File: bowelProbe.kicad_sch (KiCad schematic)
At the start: 89 parts, among them J1 Conn_01x01, J10 Conn_01x01, J11 Conn_02x03_Odd_Even, J12 Conn_01x01, J13 Conn_01x01, J2 Conn_01x01, J3 Conn_01x08, J4 Conn_01x08, J5 Conn_01x01, J6 Conn_01x01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

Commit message: Part Replacement
Replaced Coilcraft inductor for an in stock part. Adjusted PCBA files accordingly.
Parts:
- L1: value LPD5030-472MRC -> SRF0703-4R7M; footprint BowelProbe:InductorCoupled -> BowelProbe:Inductor4.7uReplacement; LCSC PN C41156791 -> C7084454; MF Coilcraft -> Bourns; Manufacturer Coilcraft -> Bourns; Manufacturer Product Number LPD5030-472MRC -> SRF0703-4R7M
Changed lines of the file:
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@@
 			)
 		)
-		(property "Value" "LPD5030-472MRC"
+		(property "Value" "SRF0703-4R7M"
 			(at 96.266 125.73 0)
 			(effects
@@
 			)
 		)
-		(property "Footprint" "BowelProbe:InductorCoupled"
-			(at 87.63 125.73 0)
-			(effects
-				(font
-					(size 1.27 1.27)
-				)
-				(justify bottom)
-				(hide yes)
-			)
-		)
-		(property "Datasheet" "https://www.coilcraft.com/getmedia/83478c05-4e24-4a3e-8ebe-bfce7101fc50/lpd5030.pdf"
-			(at 87.63 125.73 0)
-			(effects
-				(font
-					(size 1.27 1.27)
-				)
-				(hide yes)
-			)
-		)
-		(property "Description" "Coupled Inductors LPD5030 Low Profile 20% 111mOhms"
-			(at 87.63 125.73 0)
-			(effects
-				(font
-					(size 1.27 1.27)
-				)
-				(hide yes)
-			)
-		)
-		(property "MF" "Coilcraft"
+		(property "Footprint" "BowelProbe:Inductor4.7uReplacement"
+			(at 87.63 125.73 0)
+			(effects
+				(font
+					(size 1.27 1.27)
+				)
+				(justify bottom)
+				(hide yes)
+			)
+		)
+		(property "Datasheet" "https://www.bourns.com/docs/Product-Datasheets/SRF0703.pdf"
+			(at 87.63 125.73 0)
+			(effects
+				(font
+					(size 1.27 1.27)
+				)
+				(hide yes)
+			)
+		)
+		(property "Description" "3.09A 3.78A 4.7uH 40.6mΩ ±20% SMD-4P,7.6x7.6mm Power Inductors ROHS"
+			(at 87.63 125.73 0)
+			(effects
+				(font
+					(size 1.27 1.27)
+				)
+				(hide yes)
+			)
+		)
+		(property "MF" "Bourns"
 			(at 87.63 125.73 0)
 			(effects
@@
 			)
 		)
-		(property "Manufacturer" "Coilcraft"
-			(at 87.63 125.73 0)
-			(effects
-				(font
-					(size 1.27 1.27)
-				)
-				(hide yes)
-			)
-		)
-		(property "Manufacturer Product Number" "LPD5030-472MRC"
-			(at 87.63 125.73 0)
-			(effects
-				(font
-					(size 1.27 1.27)
-				)
-				(hide yes)
-			)
-		)
-		(property "LCSC PN" "C41156791"
-			(at 87.63 125.73 0)
-			(effects
+		(property "Manufacturer" "Bourns"
+			(at 87.63 125.73 0)
+			(effects
+				(font
+					(size 1.27 1.27)
+				)
+				(hide yes)
+			)
+		)
+		(property "Manufacturer Product Number" "SRF0703-4R7M"
+			(at 87.63 125.73 0)
+			(effects
+				(font
+					(size 1.27 1.27)
+				)
+				(hide yes)
+			)
+		)
+		(property "LCSC PN" "C7084454"
+			(at 87.63 125.73 0)
+			(effects

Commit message: Part Replacements
Replaced crystal and schottky diode. Adjusted schematic, PCB, and BOM accordingly. Organized schematic and colored different sections.
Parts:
- D1: footprint BowelProbe:SchottkyDiode -> BowelProbe:SchottkyReplacement; LCSC PN C6215959 -> C406049; Manufacturer Diotec Semiconductor -> Nexperia
- U1: now in the parts list
- XTAL1: value TSX-3225 16.0000MF09Z-AC3 -> TSX-3225 16.0000MF18X-AC3; LCSC PN C2650454 -> C1986974; Manufacturer Product Number TSX-3225 16.0000MF09Z-AC3 -> TSX-3225 16.0000MF18X-AC3
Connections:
- net -12V: now also L1.2; no longer L1.4
- net at C5.1, D1.A: now also L1.4; no longer L1.3
- net at C5.2, U2.3 (SW), U2.4 (SW): now also L1.3; no longer L1.2
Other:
- moved on the sheet: C1, C10, C11, C12, C13, C14, C15, C16, C17, C18, C19, C2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

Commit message: Fully Reviewed and Cleared For Immediate Order
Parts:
- U8: value MCP6002-E/MC -> MCP6002T-E/MC; LCSC PN C185041 -> C623660
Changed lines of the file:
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@@
 		(polyline
 			(pts
-				(xy 240.03 254) (xy 406.4 254) (xy 406.4 13.97) (xy 240.03 13.97)
+				(xy 19.05 166.37) (xy 62.23 166.37) (xy 62.23 147.32) (xy 143.51 147.32) (xy 143.51 13.97) (xy 19.05 13.97)
 			)
 			(stroke
 				(width 0)
 				(type solid)
-				(color 255 255 0 0.1)
+				(color 0 0 255 0.1)
 			)
 			(fill
 				(type color)
-				(color 255 255 0 0.1)
+				(color 0 0 255 0.1)
 			)
 		)
@@
 		(polyline
 			(pts
-				(xy 19.05 166.37) (xy 62.23 166.37) (xy 62.23 147.32) (xy 143.51 147.32) (xy 143.51 13.97) (xy 19.05 13.97)
+				(xy 240.03 254) (xy 406.4 254) (xy 406.4 13.97) (xy 240.03 13.97)
 			)
 			(stroke
 				(width 0)
 				(type solid)
-				(color 0 0 255 0.1)
+				(color 255 255 0 0.1)
 			)
 			(fill
 				(type color)
-				(color 0 0 255 0.1)
+				(color 255 255 0 0.1)
 			)
 		)
@@
 			)
 		)
-		(property "Value" "MCP6002-E/MC"
+		(property "Value" "MCP6002T-E/MC"
 			(at 270.51 226.06 0)
 			(effects
@@
 			)
 		)
-		(property "Description" "-40℃~+125℃ 1.8V~6V 100uA 1MHz 1pA 1pA 2 23mA 28nV/√Hz@1kHz 2uV/℃ 4.5mV 600V/ms 6V 76dB Rail-to-Rail Input, Rail-to-Rail Output DFN-8(2x3) Operational Amplifier ROHS"
+		(property "Description" "-40℃~+125℃ 1.8V~6V 100uA 1MHz 1pA 1pA 2 23mA 28nV/√Hz@1kHz 2uV/℃ 4.5mV 600V/ms 6V 76dB Rail-to-Rail Input, Rail-to-Rail Output DFN-8-EP(2x3) Operational Amplifier ROHS"
 			(at 247.65 233.68 0)
 			(effects
@@
 			)
 		)
-		(property "LCSC PN" "C185041"
+		(property "LCSC PN" "C623660"
 			(at 247.65 233.68 0)
 			(effects

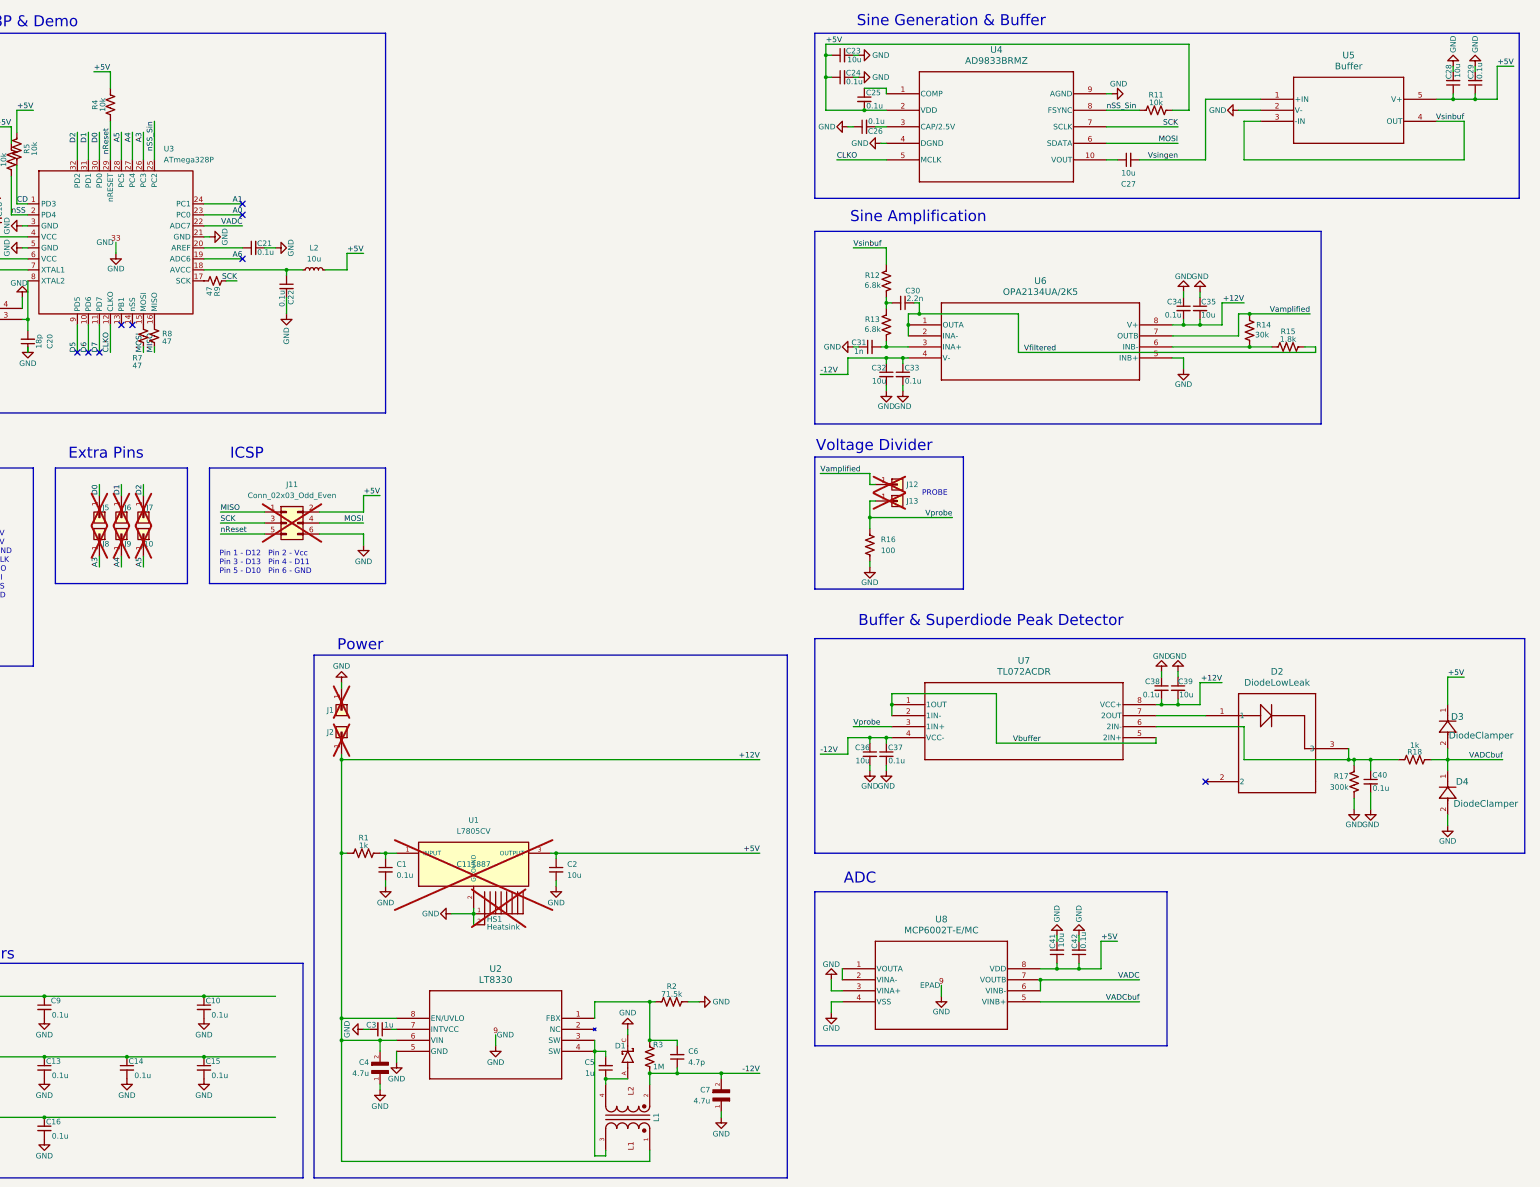
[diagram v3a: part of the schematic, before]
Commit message: Revision 1 Initial Updates
- Removed heatsink

- Swapped 5V regulator for SMT version

- Added 12V regulation

- Adjusted regulator input/output capacitors according to datasheets

- Swapped buffer for TL072 and added buffer stage between amplification and voltage divider stages

- Fixed decoupling cap issue on V- rail of buffer between sine generation and filtering

- Added test nodes to each voltage rail and to critical analog nodes
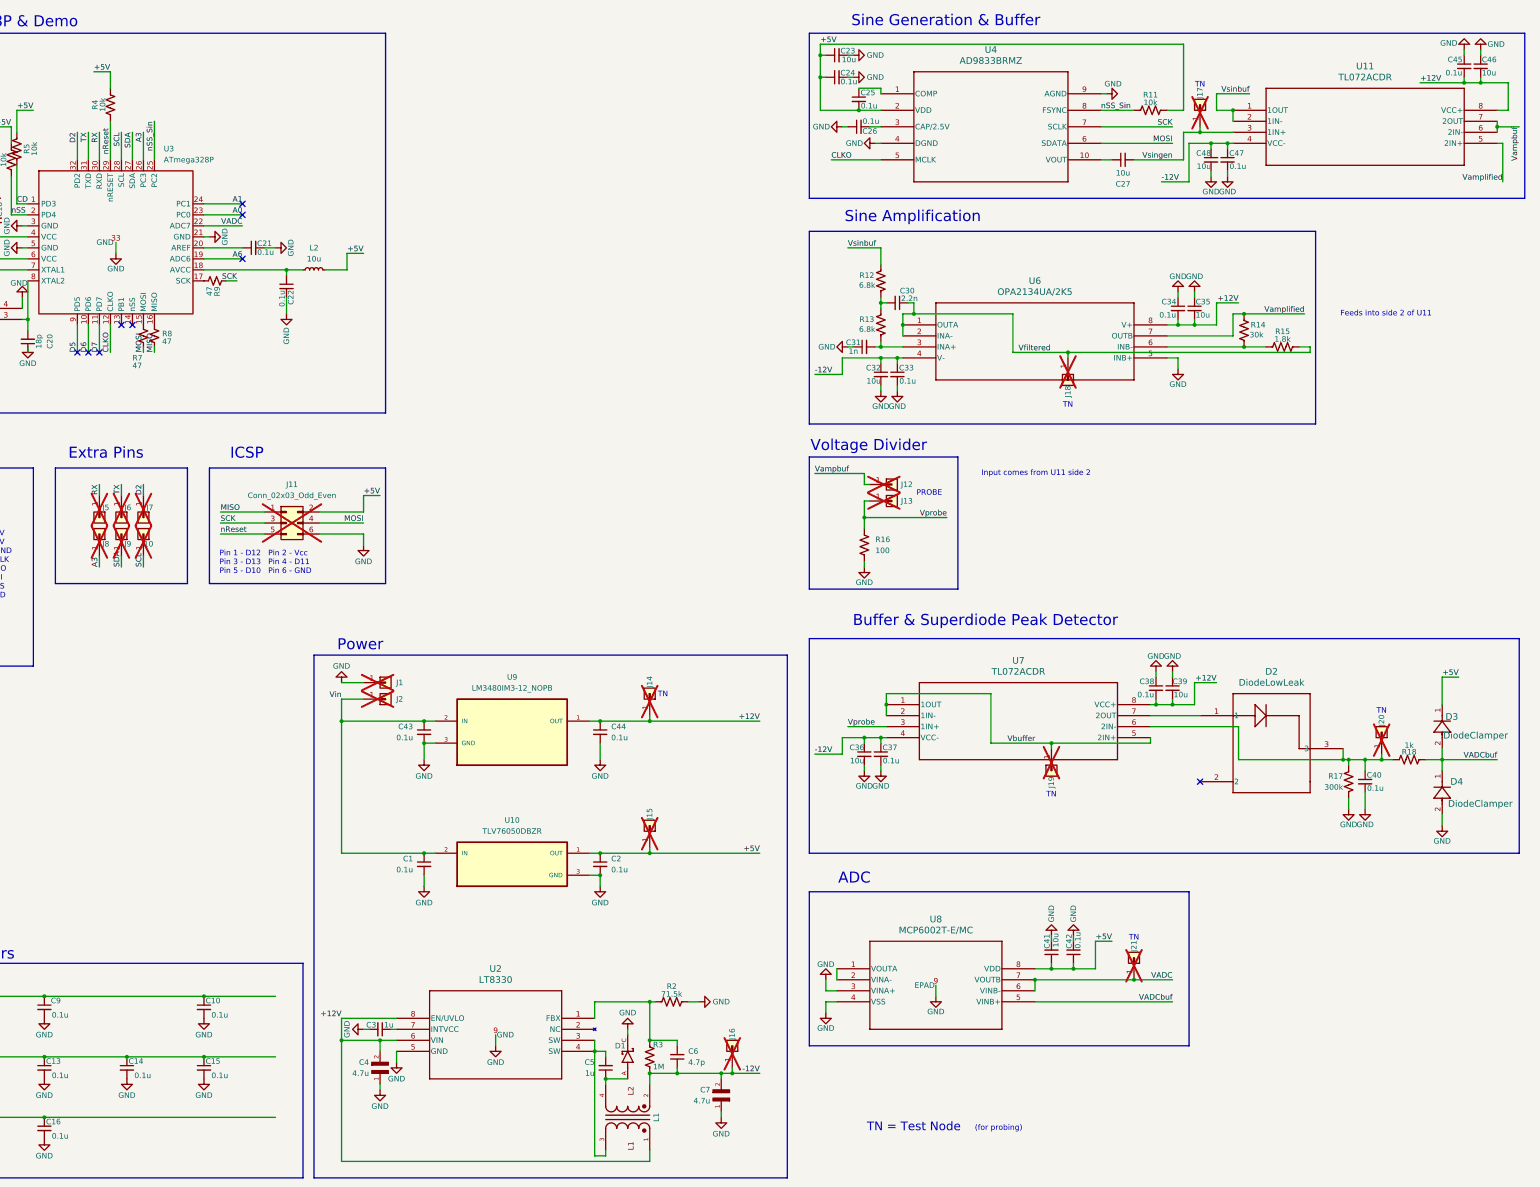
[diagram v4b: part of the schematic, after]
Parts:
- removed C28: 10u, BowelProbe:Cap10uF, symbol Device:C_Small
- removed C29: 0.1u, BowelProbe:Cap0.1uF, symbol Device:C_Small
- removed HS1: Heatsink, BowelProbe:Heatsink, symbol BowelProbe:Heatsink
- removed R1: 1k, BowelProbe:Resistor1k, symbol Device:R_US
- removed U1: L7805CV, BowelProbe:L7805CV, symbol BowelProbe:L7805CV
- removed U5: Buffer, BowelProbe:Buffer, symbol BowelProbe:Buffer
- added C43, C44, C45, C47: 0.1u, BowelProbe:Cap0.1uF, symbol Device:C_Small
- added C46, C48: 10u, BowelProbe:Cap10uF, symbol Device:C_Small
- added J14, J15, J16, J17, J18, J19, J20, J21: Conn_01x01, BowelProbe:CT3149-2, symbol Connector_Generic:Conn_01x01
- added U10: TLV76050DBZR, BowelProbe:TLV76050DBZR, symbol BowelProbe:TLV76050DBZR
- added U11: TL072ACDR, BowelProbe:TL072smd, symbol BowelProbe:TL072smd
- added U9: LM3480IM3-12_NOPB, BowelProbe:LM3480IM3-12_NOPB, symbol BowelProbe:LM3480IM3-12_NOPB
- C2: value 10u -> 0.1u; footprint BowelProbe:Cap10uF -> BowelProbe:Cap0.1uF; LCSC PN C408132 -> C85923; Manufacturer Product Number GRM155R61A106ME11D -> GRM033C71C104KE14D
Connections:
- net +12V: now also C44.1, C45.2, C46.2, J14.1 (Pin_1), U11.8 (VCC+), U9.1 (OUT); no longer J2.1 (Pin_1)
- net +5V: now also J15.1 (Pin_1), U10.1 (OUT)
- net -12V: now also C47.1, C48.1, J16.1 (Pin_1), U11.4 (VCC-)
- net GND: now also C43.2, C44.2, C45.1, C46.1, C47.2, C48.2, U10.3 (GND), U9.3 (GND)
- net VADC: now also J21.1 (Pin_1)
- net Vamplified: now also U11.5 (2IN+); no longer J12.1 (Pin_1)
- net Vbuffer: now also J19.1 (Pin_1)
- net Vfiltered: now also J18.1 (Pin_1)
- net Vsinbuf: now also U11.1 (1OUT), U11.2 (1IN-)
- net Vsingen: now also J17.1 (Pin_1), U11.3 (1IN+)
- net at C40.1, D2.3, R17.1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: now also J20.1 (Pin_1)
- net Vin: now reaches C1.1
- net Vin: now also J2.1 (Pin_1), C43.1, U10.2 (IN), U9.2 (IN)
- net A4 renamed SDA
- net A5 renamed SCL
- net D0 renamed RX
- net D1 renamed TX
- new net Vampbuf: J12.1 (Pin_1), U11.6 (2IN-), U11.7 (2OUT)
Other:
- note added: "(for probing)"
- note added: "Feeds into side 2 of U11"
- note added: "Input comes from U11 side 2"
- note added: "TN"
- note added: "TN = Test Node"
- moved on the sheet: C1, C23, C24, C25, C26, C27, C30, C31, C32, C33, C34, C35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

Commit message: Rev 1 Progress
- Updated BOM for the SMT +12V and +5V regulators

- Removed tracks from previous board

- Deleted heatsink and +5V THT regulator from layout

- Set an initial layout plan (~80% complete)

- Updated various silkscreens to signal the proper part and orientation

- Updated silkscreen for Vin, I2C, and UART pins
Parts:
- U10: LCSC PN (none) -> C2867465; Manufacturer (none) -> Texas Instruments
- U9: value LM3480IM3-12_NOPB -> LM3480IM3-12/NOPB; LCSC PN (none) -> C130175; Manufacturer (none) -> Texas Instruments
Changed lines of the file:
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@@
 		(polyline
 			(pts
-				(xy 238.76 254) (xy 406.4 253.365) (xy 406.4 13.335) (xy 238.76 13.97)
+				(xy 19.05 166.37) (xy 62.23 166.37) (xy 62.23 147.32) (xy 143.51 147.32) (xy 143.51 13.97) (xy 19.05 13.97)
 			)
 			(stroke
 				(width 0)
 				(type solid)
-				(color 255 255 0 0.1)
+				(color 0 0 255 0.1)
 			)
 			(fill
 				(type color)
-				(color 255 255 0 0.1)
+				(color 0 0 255 0.1)
 			)
 		)
@@
 		(polyline
 			(pts
-				(xy 19.05 166.37) (xy 62.23 166.37) (xy 62.23 147.32) (xy 143.51 147.32) (xy 143.51 13.97) (xy 19.05 13.97)
+				(xy 238.76 254) (xy 406.4 253.365) (xy 406.4 13.335) (xy 238.76 13.97)
 			)
 			(stroke
 				(width 0)
 				(type solid)
-				(color 0 0 255 0.1)
+				(color 255 255 0 0.1)
 			)
 			(fill
 				(type color)
-				(color 0 0 255 0.1)
+				(color 255 255 0 0.1)
 			)
 		)
@@
 			)
 		)
-		(property "Value" "LM3480IM3-12_NOPB"
+		(property "Value" "LM3480IM3-12/NOPB"
 			(at 171.45 170.18 0)
 			(effects
@@
 			)
 		)
-		(property "Description" ""
+		(property "Description" "-40℃~+125℃@(Tj) 1 1.2V@(100mA) 100mA 12V 30V 360uVrms Fixed Over Current Protection Positive SOT-23 Voltage Regulators - Linear, Low Drop Out (LDO) Regulators ROHS"
 			(at 171.45 177.8 0)
 			(effects
@@
 			)
 		)
+		(property "LCSC PN" "C130175"
+			(at 171.45 177.8 0)
+			(effects
+				(font
+					(size 1.27 1.27)
+				)
+				(hide yes)
+			)
+		)
+		(property "Manufacturer" "Texas Instruments"
+			(at 171.45 177.8 0)
+			(effects
+				(font
+					(size 1.27 1.27)
+				)
+				(hide yes)
+			)
+		)
 		(pin "1"
 		)
@@
 			)
 		)
-		(property "Description" ""
+		(property "Description" "-40℃~+125℃@(Tj) 1 1.2V@(100mA) 100mA 30V 5V 5mA Fixed Over Current Protection、Over Temperature Protection Positive SOT-23 Voltage Regulators - Linear, Low Drop Out (LDO) Regulators ROHS"
 			(at 171.45 210.82 0)
 			(effects
@@
 				(hide yes)
 			)
+		)
+		(property "LCSC PN" "C2867465"
+			(at 171.45 210.82 0)
+			(effects
+				(font
+					(size 1.27 1.27)
+				)
+				(hide yes)
+			)
+		)
+		(property "Manufacturer" "Texas Instruments"
+			(at 171.45 210.82 0)
+			(effects
+				(font
+					(size 1.27 1.27)
+				)
+				(hide yes)
+			)
